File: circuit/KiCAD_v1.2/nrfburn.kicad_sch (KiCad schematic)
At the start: 30 parts, among them IC1 ATMEGA88PA-AU, P1 PWR_5V, P2 USB_B, P3 SWD, U1 AVR-ISP6, U2 MCP1702, U3 LU1_PRG_SPRKFN, U4 LU1_PRG_DNGL, U5 LE1_PRG, U6 DBG_LU1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

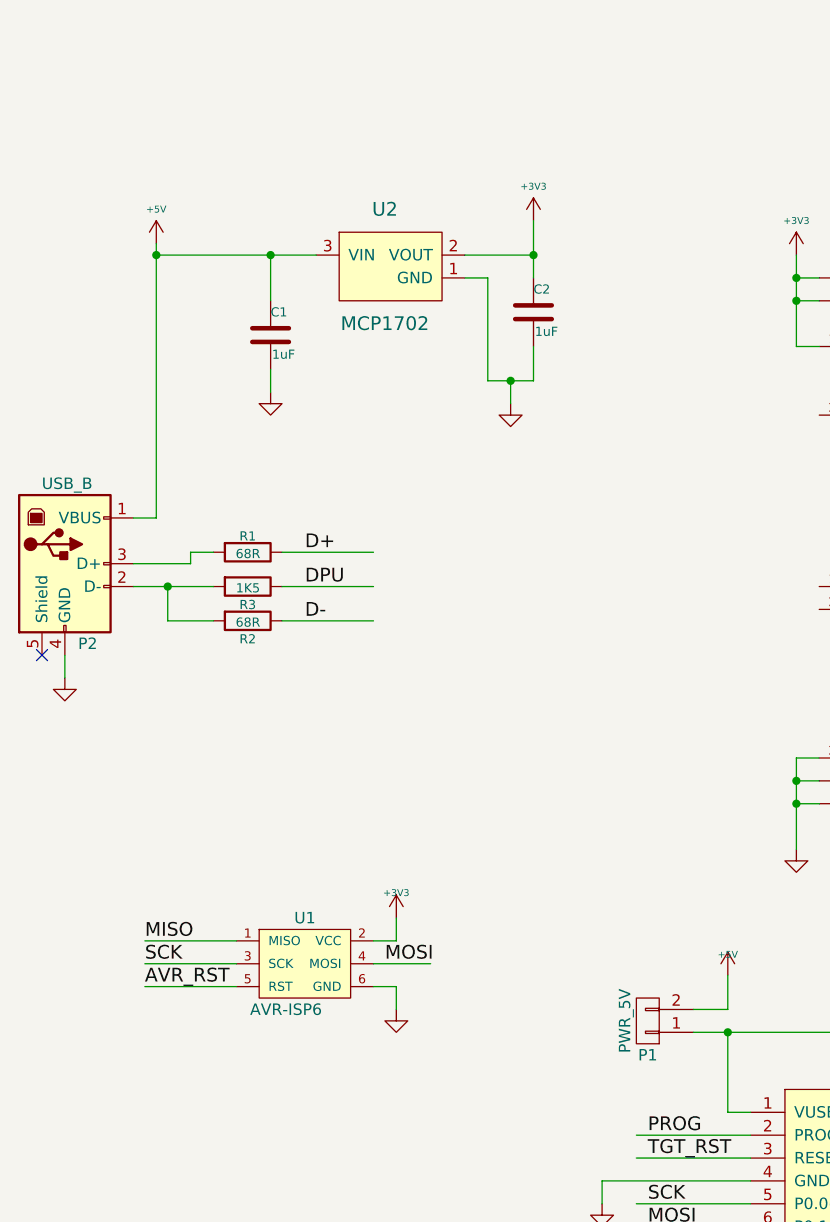
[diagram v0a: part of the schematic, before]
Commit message: added 3D models
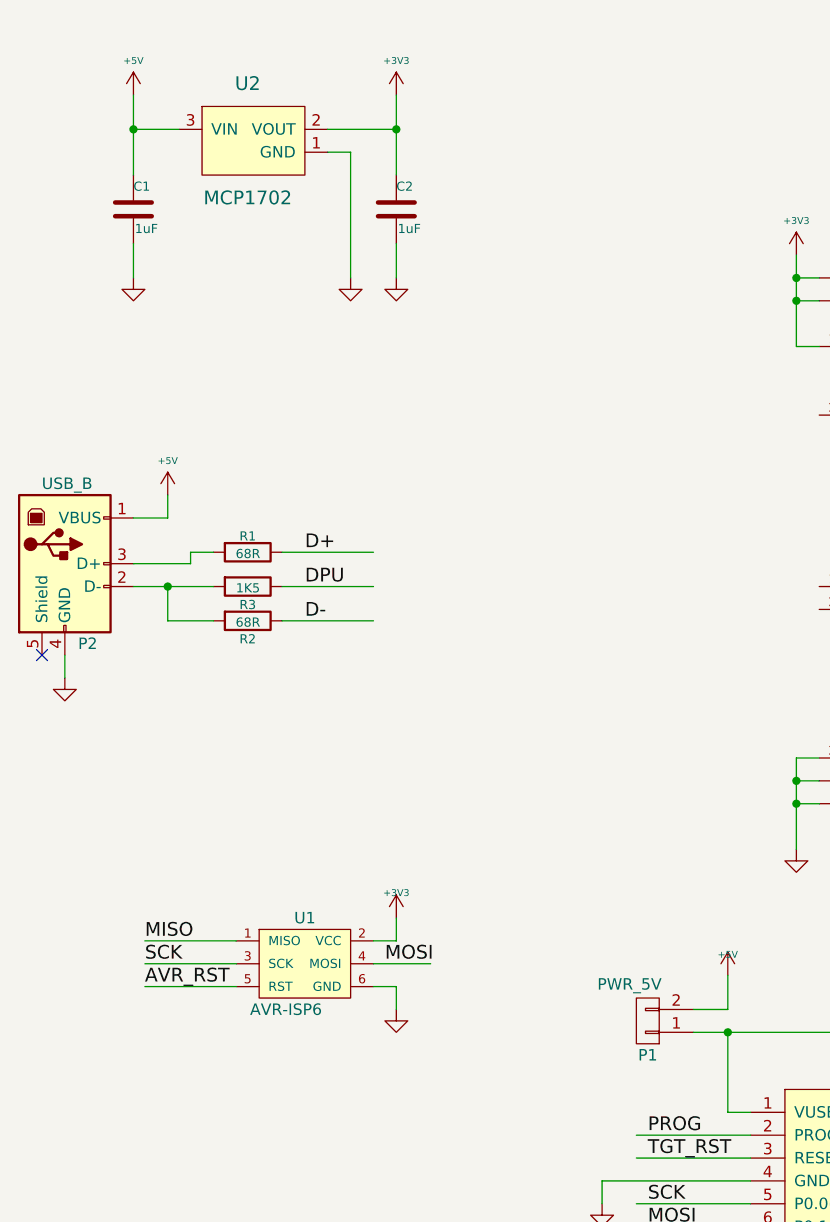
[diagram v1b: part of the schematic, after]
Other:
- moved on the sheet: C1, C2, U2
